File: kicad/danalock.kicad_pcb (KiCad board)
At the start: 2 copper layers, 25.4 x 31.6 mm, 11 parts, among them J1 Conn_01x02, J2 Conn_01x07, J3 Conn_01x03, U1 ESP32mini_shield_inner, U2 DSN-MINI-360

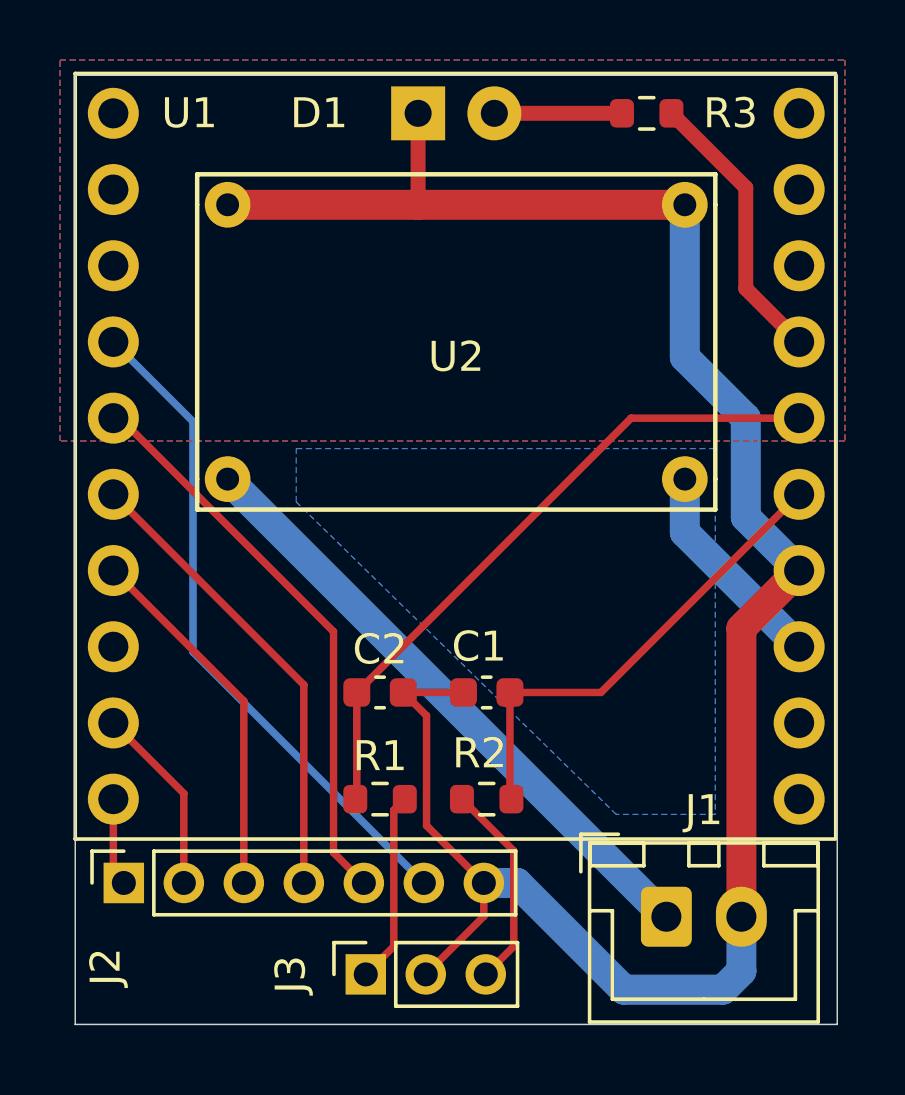
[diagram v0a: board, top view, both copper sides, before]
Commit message: Fix orientation, add missing 3V3 pin.
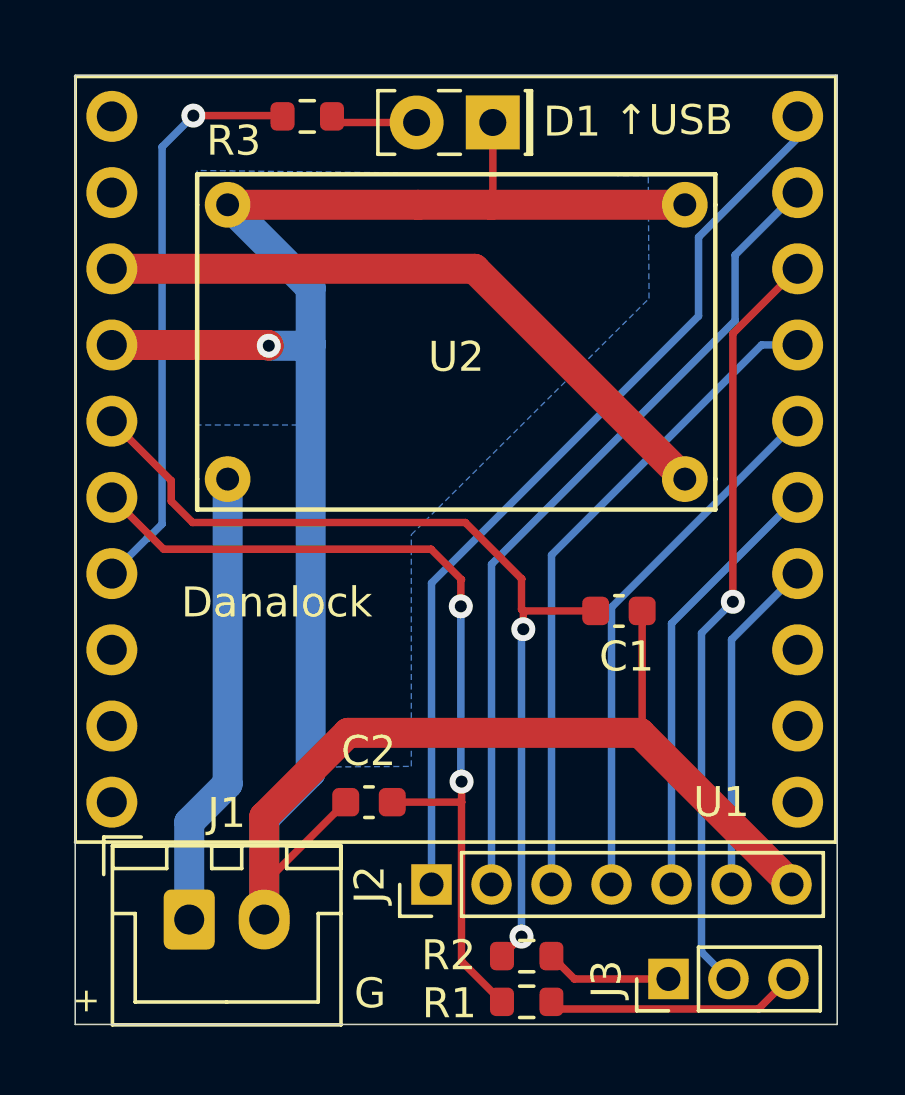
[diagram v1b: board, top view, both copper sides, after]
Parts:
- D1: footprint LED_THT:LED_D5.0mm -> LED_THT:LED_Rectangular_W5.0mm_H2.0mm
- J2: footprint Connector_PinSocket_2.00mm:PinSocket_1x07_P2.00mm_Vertical -> Connector_PinHeader_2.00mm:PinHeader_1x07_P2.00mm_Vertical
- J3: footprint Connector_PinSocket_2.00mm:PinSocket_1x03_P2.00mm_Vertical -> Connector_PinHeader_2.00mm:PinHeader_1x03_P2.00mm_Vertical
- moved U1 36.1 mm to (144.7, 110.6), turned to 180 degrees
- moved J1 15.9 mm to (121.9, 114.5)
- moved R3 11.3 mm to (125.8, 87.7), turned to 180 degrees
- moved J2 10.3 mm to (130.0, 113.3)
- moved J3 10.1 mm to (137.9, 116.5)
- moved R1 8.34 mm to (133.2, 117.2)
- moved R2 5.40 mm to (133.2, 115.7), turned to 0 degrees
- moved C1 5.18 mm to (136.2, 104.2), turned to 0 degrees
- moved C2 3.68 mm to (127.9, 110.6), turned to 180 degrees
- moved D1 2.51 mm to (132.0, 87.9), turned to 180 degrees
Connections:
- J3 pad 1: Net-(J3-Pad1) -> Net-(J3-Pin_1)
- J3 pad 2: GND -> +3V3
- J3 pad 3: Net-(J3-Pad3) -> Net-(J3-Pin_3)
- R1 pad 2: Net-(J3-Pad1) -> Net-(J3-Pin_3)
- R2 pad 2: Net-(J3-Pad3) -> Net-(J3-Pin_1)
- U1 pad 16: unconnected-(U1-Pad16) -> +3V3
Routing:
- net ENC_A: track 2.94 -> 30.7 mm
- net +3V3: track 0.00 -> 25.4 mm, vias 0 -> 1
- net ENC_B: track 6.31 -> 27.3 mm
- net HANDLE_SW: track 16.0 -> 31.8 mm, vias 0 -> 2
- net +5V: track 7.17 -> 22.0 mm
- net GND: track 69.8 -> 83.6 mm, vias 0 -> 1
- net STBY: track 22.3 -> 11.3 mm
- net LED: track 9.38 -> 19.4 mm, vias 0 -> 1
- net IN1: track 12.2 -> 22.1 mm
- net Net-(J3-Pin_3): track 0.00 -> 8.41 mm
- net DOOR_SW: track 22.1 -> 29.8 mm, vias 0 -> 2
- net Net-(J3-Pad3): track 6.95 -> 0.00 mm
- net Net-(J3-Pad1): track 6.38 -> 0.00 mm
- net +12V: track 20.7 -> 15.2 mm
- net PWM: track 19.1 -> 14.6 mm
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- removed copper zone on B.Cu, net +5V
- removed copper zone on F.Cu, net GND
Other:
- board text added: "+"
- board text added: "Danalock"
- board text added: "G"
- board text added: "https://github.com/bullestock/danalock-wired"
- board text added: "↑USB"
